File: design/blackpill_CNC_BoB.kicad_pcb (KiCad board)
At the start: 4 copper layers, 304 parts, among them J101 ALimIN, J102 ZLimIN, J103 YLimIN, J104 XLimIN, J105 CS_IN, J106 FH_IN, J107 DoorIN, J108 ResetIN, J109 ProbeIN, J110 12V Power in, J111 AuxEncIn, J112 5V Power out, J113 ADC_in_1, J114 ADC_in_2, J115 stepDriverLim, J116 Reset, J117 UART1, J118 I2C, J119 SpindleVFD, J120 Spindle/Coolant, J121 Spindle, J122 Coolant, J123 AuxOut, J124 XStepDrv, J125 YStepDrv, J126 ZStepDrv, J127 AStepDrv, J128 Driver Power in/out, J129 Relais Power in/out, J130 Conn_02x03_Odd_Even, J131 Conn_02x03_Odd_Even, U101 TLP290-4, U102 TLP290-4, U103 TLP290-4, U104 74LVC2G17, U105 LD1117S50TR_SOT223, U106 LM358, U107 TLV9001, U108 TLV9001, U109 YAAJ_WeAct_BlackPill_Part_Like, U110 TLV9001, U111 TLV9001, U112 74HCT541, U113 74HCT541, U114 74HCT541, U115 ULN2003A, U116 ULN2003A, U117 ULN2003A

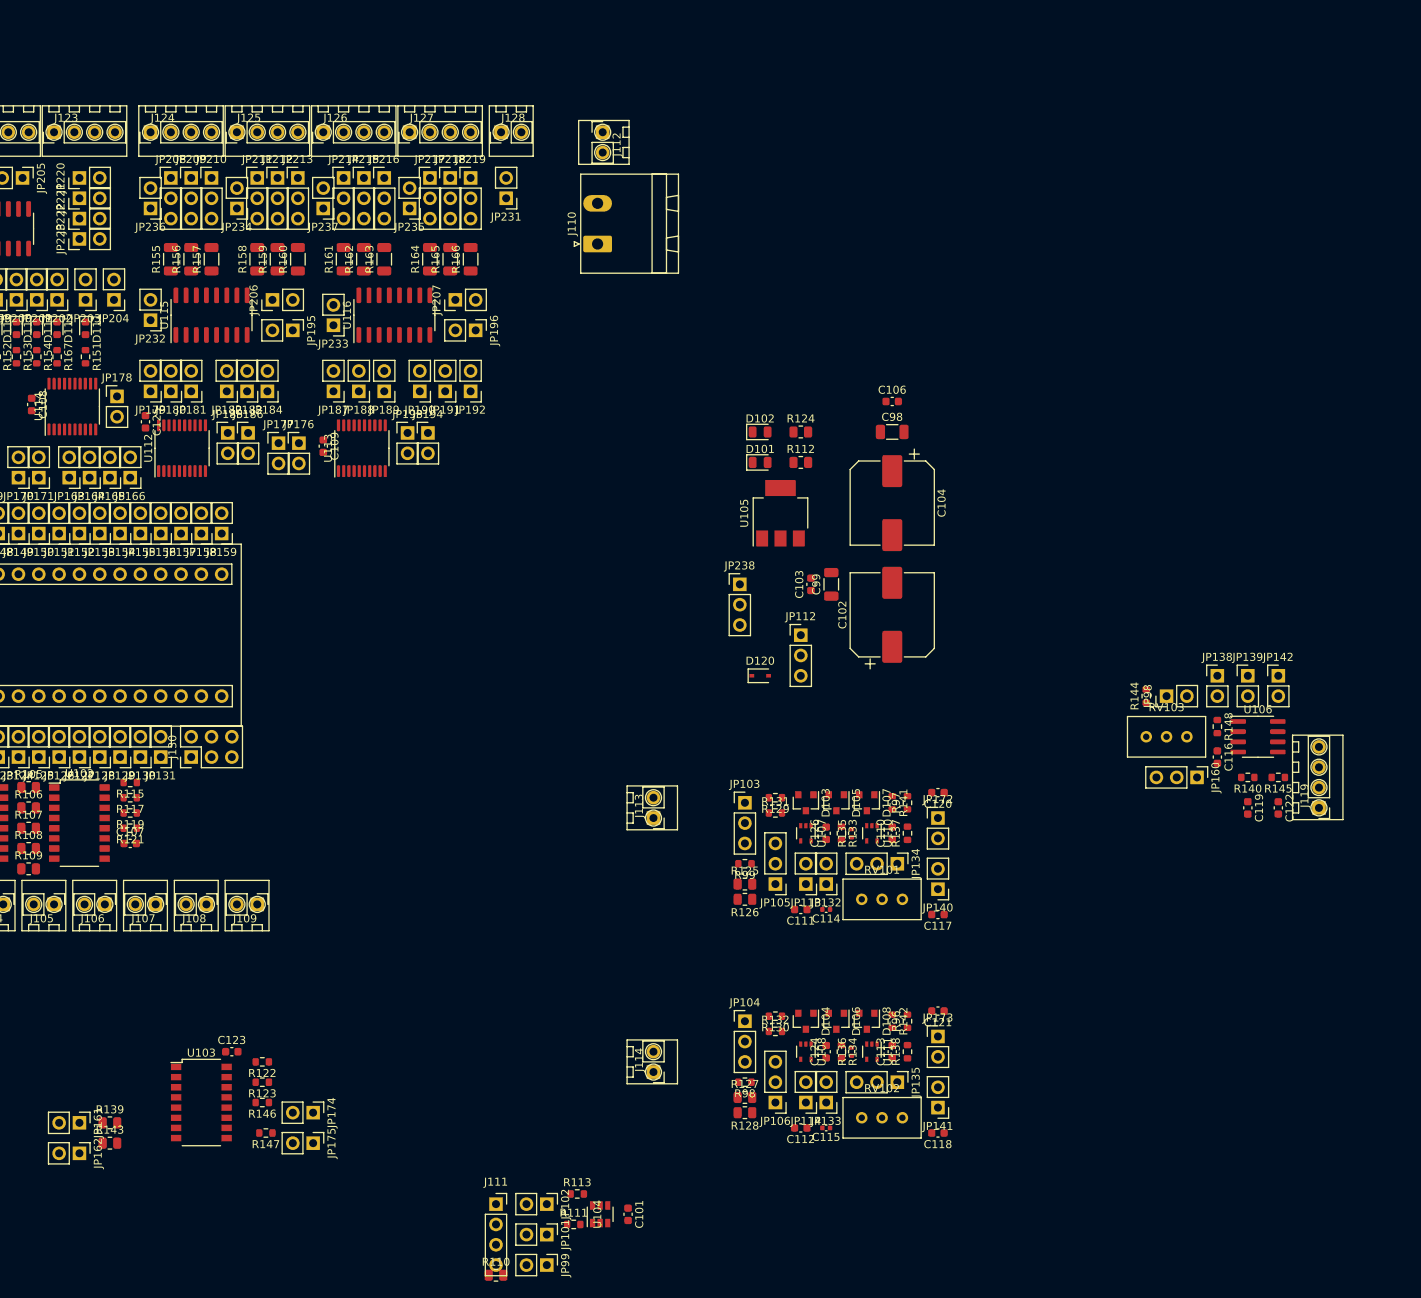
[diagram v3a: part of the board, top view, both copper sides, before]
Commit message: placed aux in
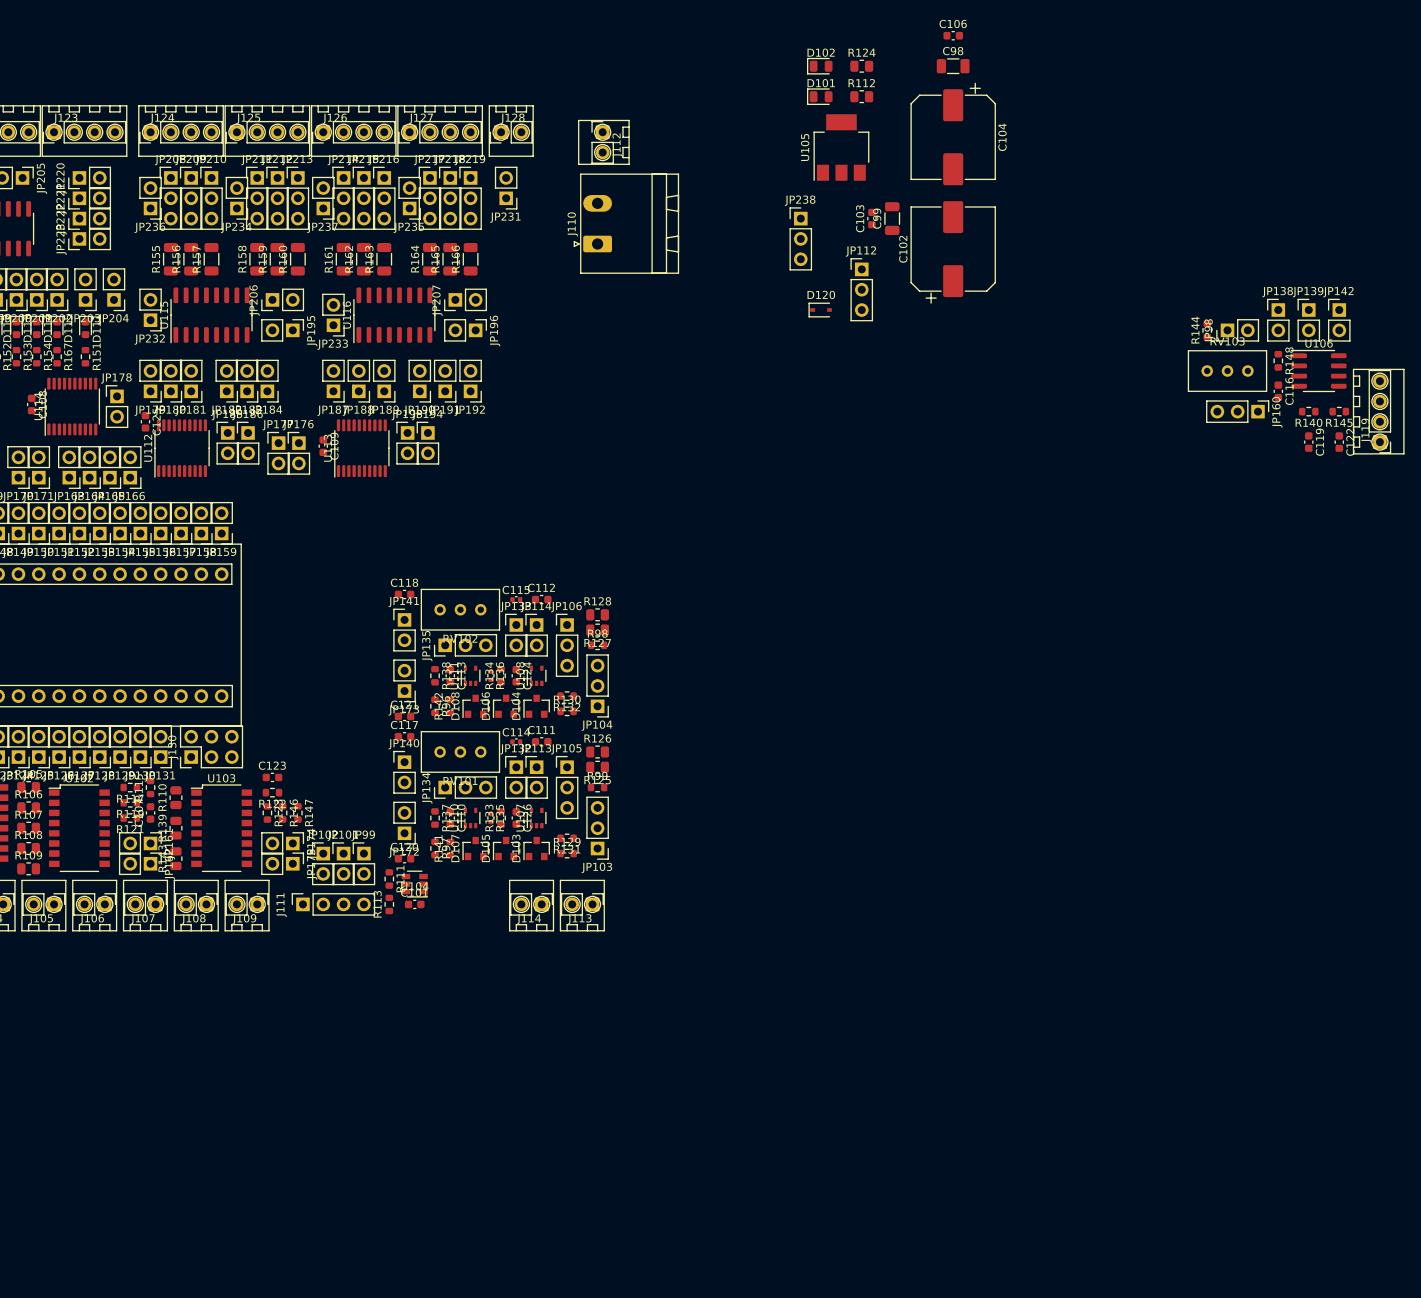
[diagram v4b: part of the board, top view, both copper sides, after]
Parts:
- moved C118 94.7 mm to (73.7, 59.7), turned to 0 degrees
- moved JP141 90.3 mm to (73.7, 62.9), turned to 0 degrees
- moved RV102 85.9 mm to (78.1, 61.6), turned to 180 degrees
- moved JP173 79.4 mm to (73.7, 71.8), turned to 180 degrees
- moved JP135 78.6 mm to (78.7, 66.0), turned to 90 degrees
- moved C115 76.6 mm to (87.6, 60.3), turned to 0 degrees
- moved C121 76.2 mm to (73.7, 74.9), turned to 0 degrees
- moved R138 75.5 mm to (77.5, 69.8), turned to 270 degrees
- moved C112 73.6 mm to (90.8, 60.3), turned to 0 degrees
- moved C113 72.5 mm to (79.4, 69.8), turned to 270 degrees
- moved R110 71.9 mm to (45.1, 85.1), turned to 90 degrees
- moved JP133 71.2 mm to (87.6, 63.5), turned to 0 degrees
- moved R96 71.0 mm to (77.5, 73.7), turned to 270 degrees
- moved C117 70.3 mm to (73.7, 77.5), turned to 0 degrees
- moved U111 68.7 mm to (81.9, 69.8), turned to 90 degrees
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
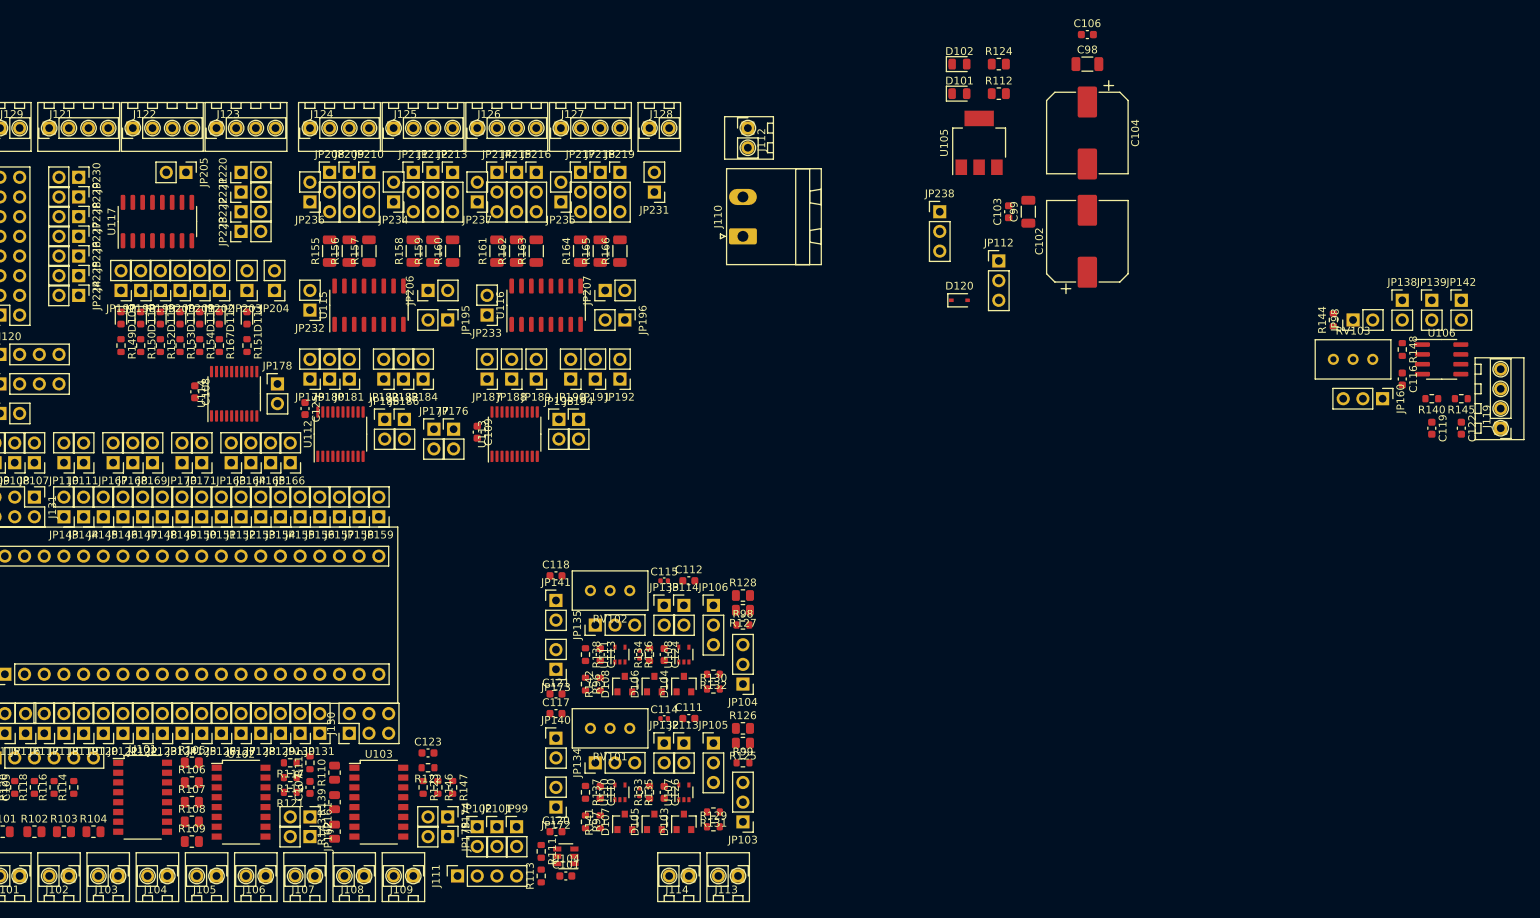
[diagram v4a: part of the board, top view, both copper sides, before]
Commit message: placed power
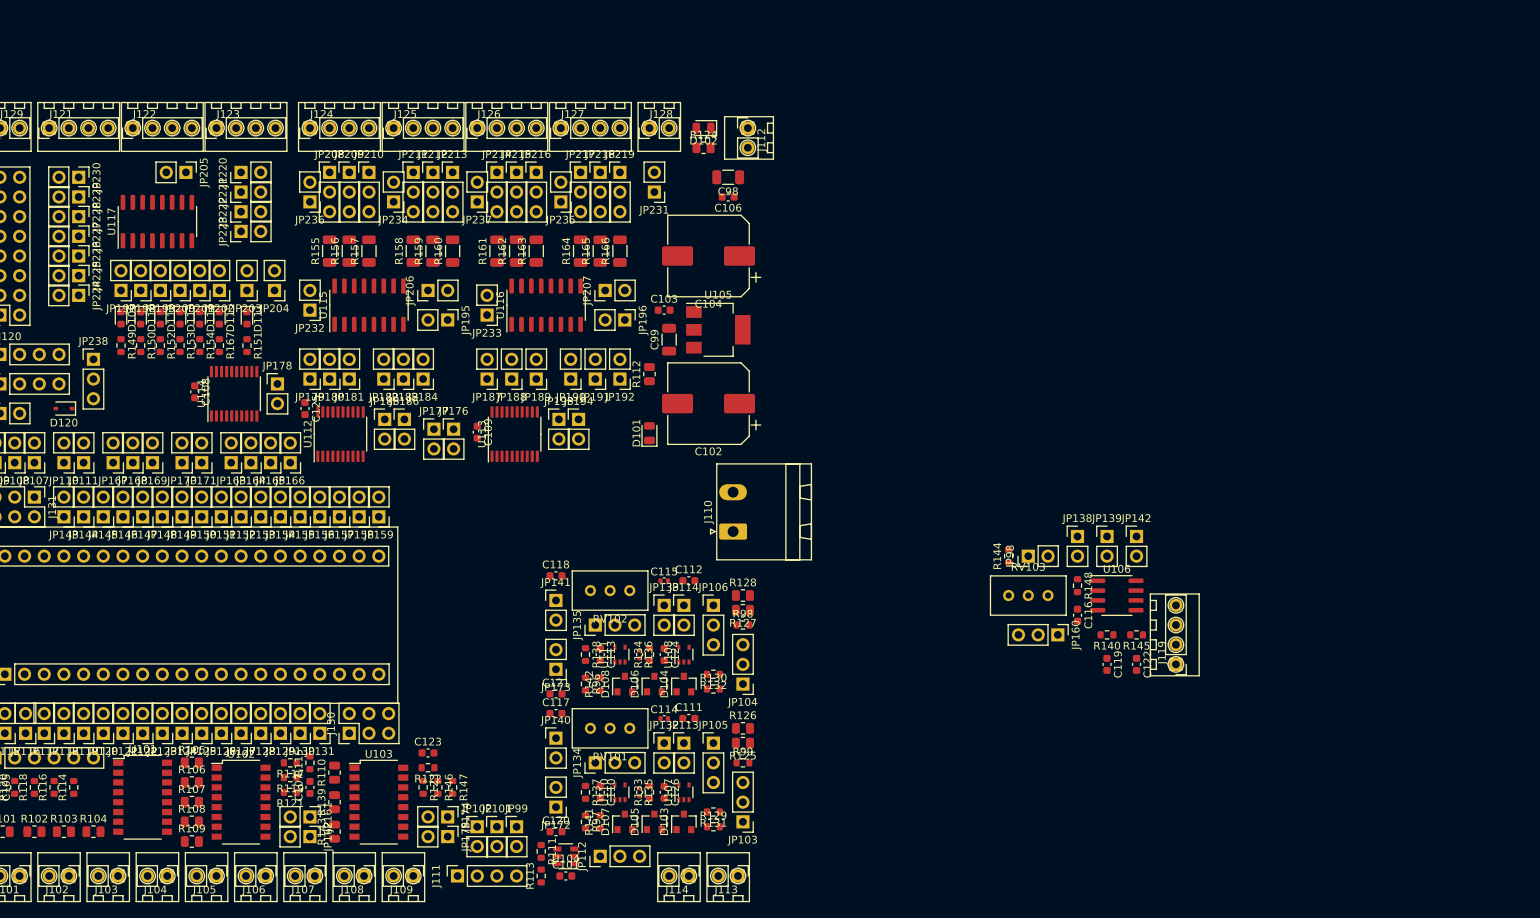
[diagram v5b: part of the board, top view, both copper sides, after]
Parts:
- moved D120 116.4 mm to (10.2, 38.1), turned to 180 degrees
- moved JP238 110.9 mm to (14.0, 31.8)
- moved JP112 92.5 mm to (79.4, 95.9), turned to 90 degrees
- moved D101 59.3 mm to (85.7, 41.3), turned to 90 degrees
- moved R112 57.8 mm to (85.7, 33.7), turned to 90 degrees
- moved C102 53.2 mm to (93.3, 37.5), turned to 180 degrees
- moved J119 51.8 mm to (153.7, 71.1)
- moved C116 51.8 mm to (141.0, 64.8)
- moved C119 51.8 mm to (144.8, 71.1)
- moved C122 51.8 mm to (148.6, 71.1)
- moved JP138 51.8 mm to (141.0, 54.6)
- moved JP139 51.8 mm to (144.8, 54.6)
- moved JP142 51.8 mm to (148.6, 54.6)
- moved JP160 51.8 mm to (138.4, 67.3)
- moved JP98 51.8 mm to (134.6, 57.1)
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
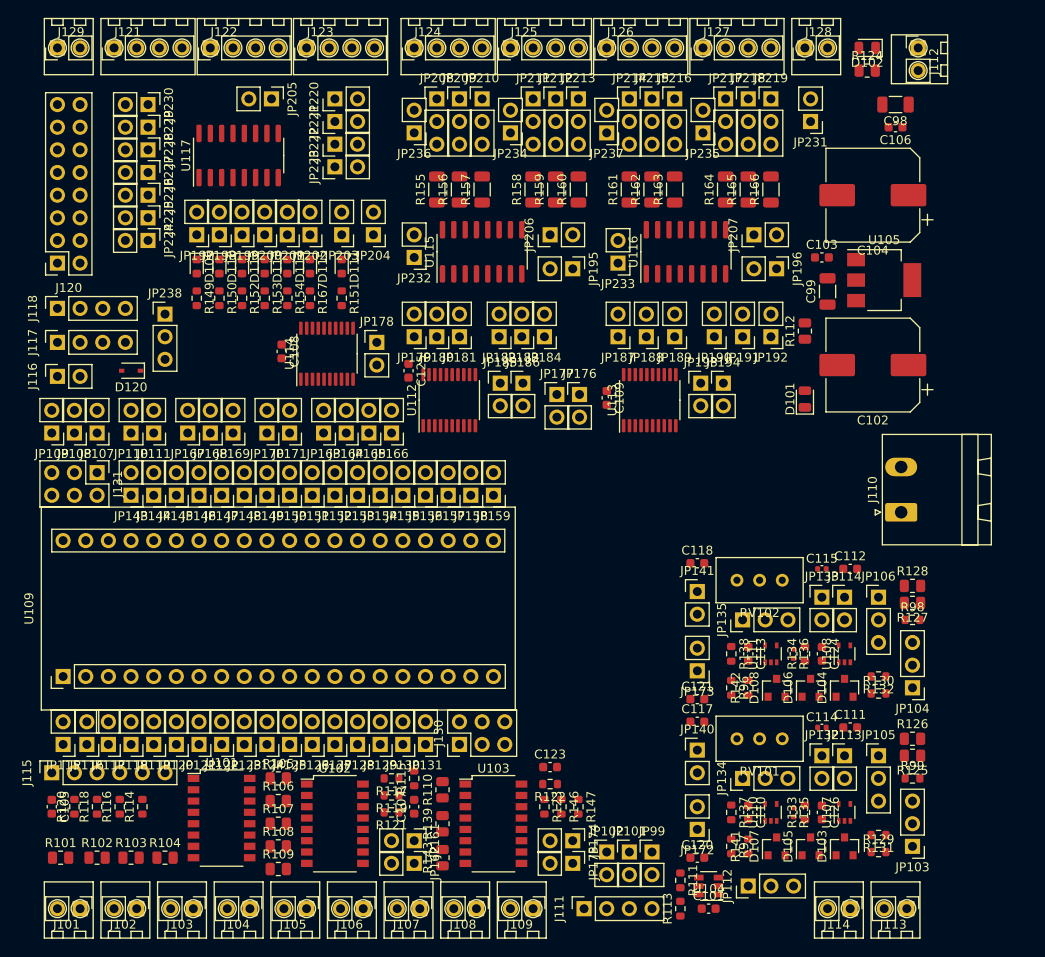
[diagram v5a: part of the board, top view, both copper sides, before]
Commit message: placed mount holes
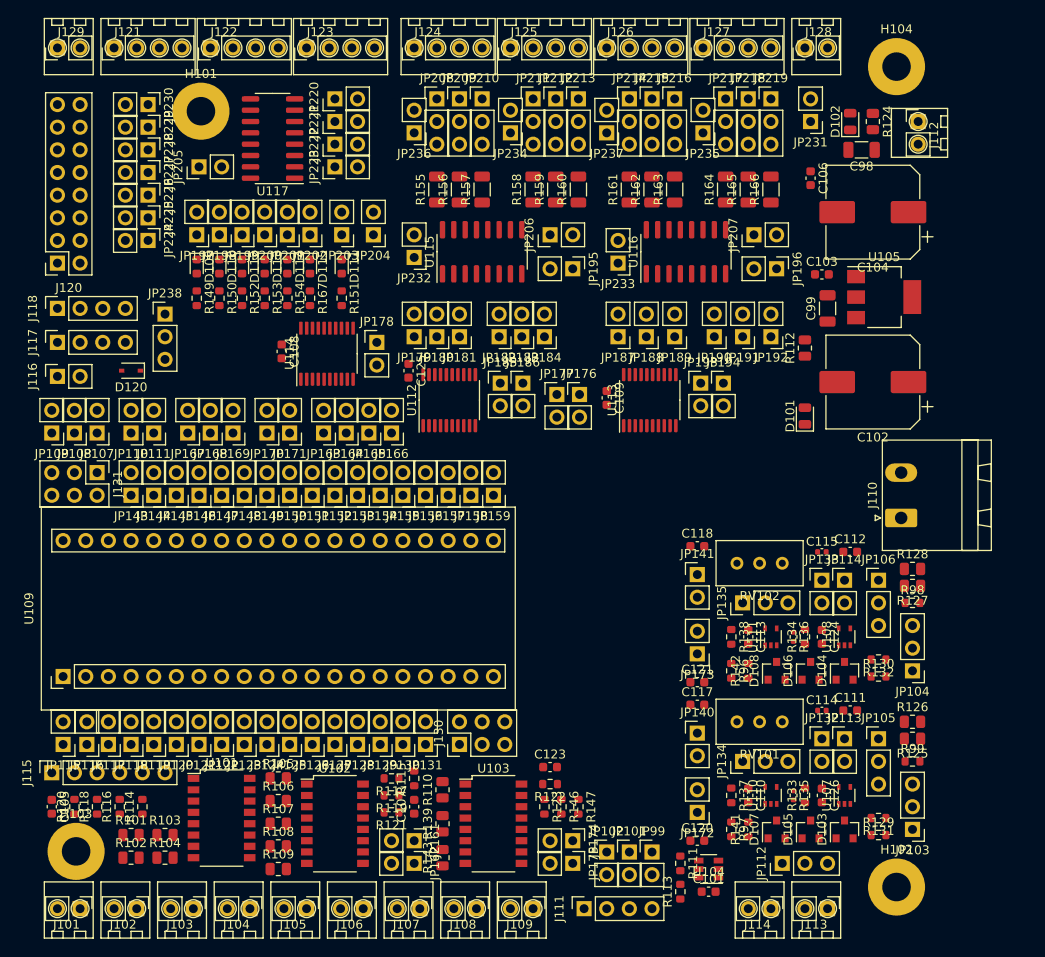
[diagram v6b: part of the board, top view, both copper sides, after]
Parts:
- added H101: MountingHole_Pad, MountingHole:MountingHole_3.2mm_M3_Pad, F.Cu at (18.0, 9.00)
- added H102: MountingHole_Pad, MountingHole:MountingHole_3.2mm_M3_Pad, F.Cu at (96.0, 96.0)
- added H103: MountingHole_Pad, MountingHole:MountingHole_3.2mm_M3_Pad, F.Cu at (4.00, 92.0)
- added H104: MountingHole_Pad, MountingHole:MountingHole_3.2mm_M3_Pad, F.Cu at (96.0, 4.00)
- moved JP205 11.1 mm to (17.8, 15.2), turned to 90 degrees
- moved C106 11.1 mm to (86.4, 16.5), turned to 270 degrees
- moved J113 8.89 mm to (88.3, 98.4)
- moved J114 8.89 mm to (81.9, 98.4)
- moved D102 8.47 mm to (90.8, 10.2), turned to 90 degrees
- moved R101 8.30 mm to (10.2, 90.2)
- moved J112 8.26 mm to (98.4, 10.2)
- moved C98 6.35 mm to (92.1, 13.3)
- moved R124 5.75 mm to (93.3, 10.2), turned to 270 degrees
- moved JP112 4.58 mm to (83.2, 93.3)
- moved R103 4.58 mm to (14.0, 90.2)
- moved U117 4.26 mm to (26.0, 12.1), turned to 180 degrees
- moved R102 3.81 mm to (10.2, 92.7)
- moved R127 1.91 mm to (97.8, 62.2)
- moved C101 1.91 mm to (74.9, 96.5)
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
